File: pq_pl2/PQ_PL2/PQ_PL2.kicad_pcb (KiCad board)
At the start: 4 copper layers, 40 x 40 mm, 79 parts, among them J1 BBL-110-Y-X, J2 BBL-110-Y-X, J3 BBL-110-Y-X, J4 BBL-110-Y-X, J5 U.FL-R-SMT, J6 MS-156C3, J7 MS-156C3, J8 U.FL-R-SMT, U1 LEE2-6+, U2 MAX2121, U4 LT3048, U5 LT071DBV, Y1 ECS-TXO-2016MV

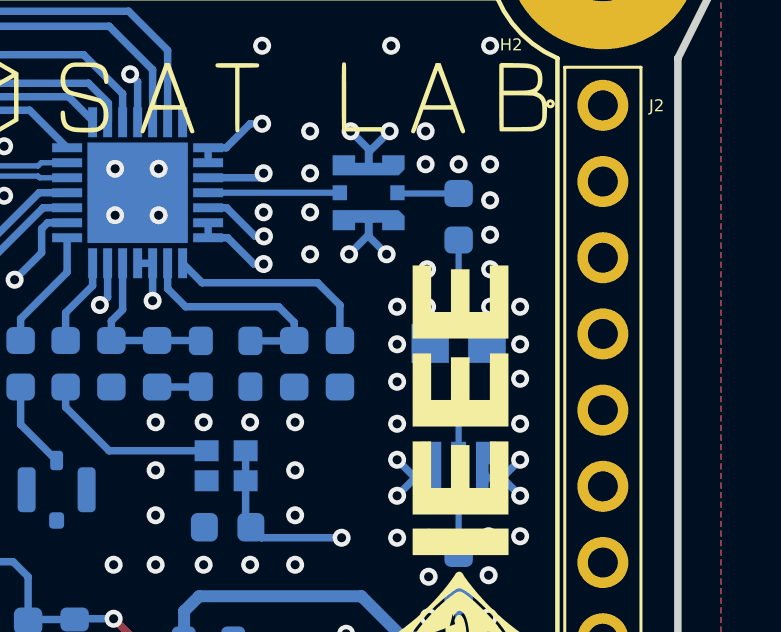
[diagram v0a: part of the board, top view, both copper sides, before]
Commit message: Payload 2 V3.2 - Rounded the RF 90 degree turn between the C3 and J8 probe connector
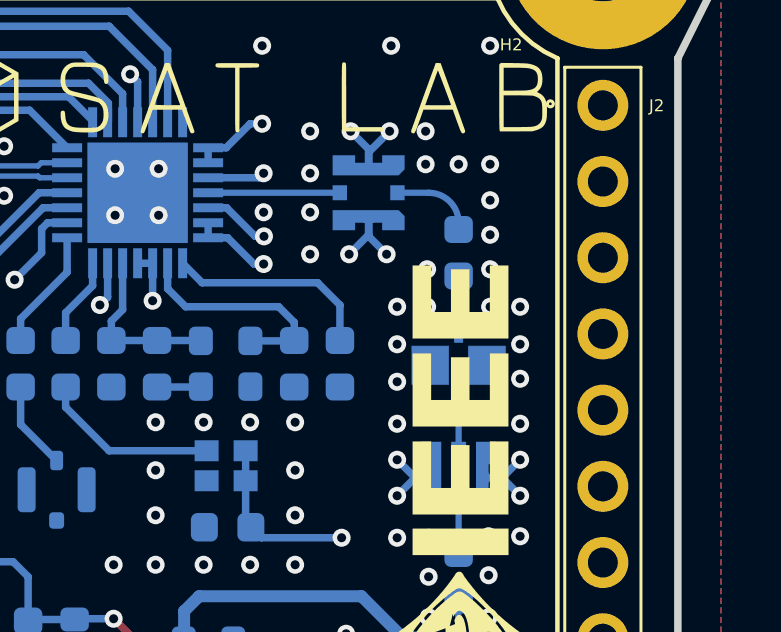
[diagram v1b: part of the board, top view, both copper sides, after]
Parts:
- moved C3 1.20 mm to (114.8, 52.6)
- moved FL1 0.73 mm to (114.8, 56.4)
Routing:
- net RF: track 2.05 -> 2.80 mm
- net Net-(FL1-IN): track 2.11 -> 1.41 mm
- net Net-(FL1-Out): track 2.11 -> 1.60 mm
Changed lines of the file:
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@@
   )
   (footprint "-nsl_rf:GE0805C-3" (layer "B.Cu")
-    (at 114.75 55.625 90)
+    (at 114.75 56.35 90)
     (property "Sheetfile" "PQ_PL2.kicad_sch")
     (property "Sheetname" "")
@@
   )
   (footprint "Capacitor_SMD:C_0603_1608Metric" (layer "B.Cu")
-    (at 114.75 51.4 90)
+    (at 114.75 52.6 90)
     (descr "Capacitor SMD 0603 (1608 Metric), square (rectangular) end terminal, IPC_7351 nominal, (Body size source: IPC-SM-782 page 76, https://www.pcb-3d.com/wordpress/wp-content/uploads/ipc-sm-782a_amendment_1_and_2.pdf), generated with kicad-footprint-generator")
     (tags "capacitor")
@@
   (gr_line locked (start 88.043 46.1172) (end 88.043 72.1172)
     (stroke (width 0.15) (type solid)) (layer "F.SilkS"))
+  (gr_line (start 112.7625 50.6) (end 113.7375 50.6)
+    (stroke (width 0.61) (type default)) (layer "B.Mask"))
   (gr_line (start 114.75 65.6) (end 114.75 66.7)
     (stroke (width 0.64) (type default)) (layer "B.Mask"))
-  (gr_line (start 112.8 50.6) (end 114.875 50.6)
-    (stroke (width 0.64) (type default)) (layer "B.Mask"))
+  (gr_arc (start 113.5 50.565167) (mid 114.462448 50.906475) (end 114.852851 51.850076)
+    (stroke (width 0.6) (type default)) (layer "B.Mask"))
   (gr_line (start 114.75 69.25) (end 114.75 70.35)
     (stroke (width 0.64) (type default)) (layer "B.Mask"))
@@
   (gr_line (start 114.75 61.15) (end 114.75 62.75)
     (stroke (width 0.64) (type default)) (layer "B.Mask"))
-  (gr_line (start 114.75 52.05) (end 114.75 54.55)
+  (gr_line (start 114.75 53.25) (end 114.75 55.3)
     (stroke (width 0.61) (type default)) (layer "B.Mask"))
-  (gr_line (start 114.75 56.7) (end 114.75 59.05)
+  (gr_line (start 114.75 57.4) (end 114.75 59.05)
     (stroke (width 0.64) (type default)) (layer "B.Mask"))
   (gr_line (start 114.75 71.9) (end 114.75 73.05)
@@
   (segment (start 114.7375 65.7) (end 114.7375 64.1875) (width 0.21) (layer "B.Cu") (net 3))
   (segment (start 114.75 61.06) (end 114.75 62.625) (width 0.21) (layer "B.Cu") (net 4))
-  (segment (start 114.75 52.175) (end 114.75 54.28) (width 0.21) (layer "B.Cu") (net 5))
-  (segment (start 114.75 50.625) (end 112.735 50.625) (width 0.21) (layer "B.Cu") (net 6))
-  (segment (start 112.735 50.625) (end 112.71 50.6) (width 0.21) (layer "B.Cu") (net 6))
+  (segment (start 114.75 53.375) (end 114.75 54.975) (width 0.21) (layer "B.Cu") (net 5))
+  (segment (start 113.75 50.6) (end 112.71 50.6) (width 0.21) (layer "B.Cu") (net 6))
+  (segment (start 114.75 51.6) (end 114.75 51.825) (width 0.21) (layer "B.Cu") (net 6))
+  (arc (start 114.75 51.6) (mid 114.457106 50.892893) (end 113.75 50.6) (width 0.21) (layer "B.Cu") (net 6))
   (via (at 103.8 46.65) (size 0.6) (drill 0.3) (layers "F.Cu" "B.Cu") (net 7))
   (via (at 99.95 53.5) (size 0.6) (drill 0.3) (layers "F.Cu" "B.Cu") (net 7))
@@
   (segment (start 107.187 68.59) (end 107.187 67.066) (width 0.4) (layer "B.Cu") (net 31))
   (segment (start 107.187 67.066) (end 107.187 65.581) (width 0.4) (layer "B.Cu") (net 31))
-  (segment (start 114.75 59.14) (end 114.75 57.03) (width 0.21) (layer "B.Cu") (net 32))
+  (segment (start 114.75 57.725) (end 114.75 59.14) (width 0.21) (layer "B.Cu") (net 32))
   (segment (start 103.1 45.05) (end 94.0528 45.05) (width 0.25) (layer "B.Cu") (net 33))
   (segment (start 104.55 48.25) (end 104.55 46.5) (width 0.25) (layer "B.Cu") (net 33))

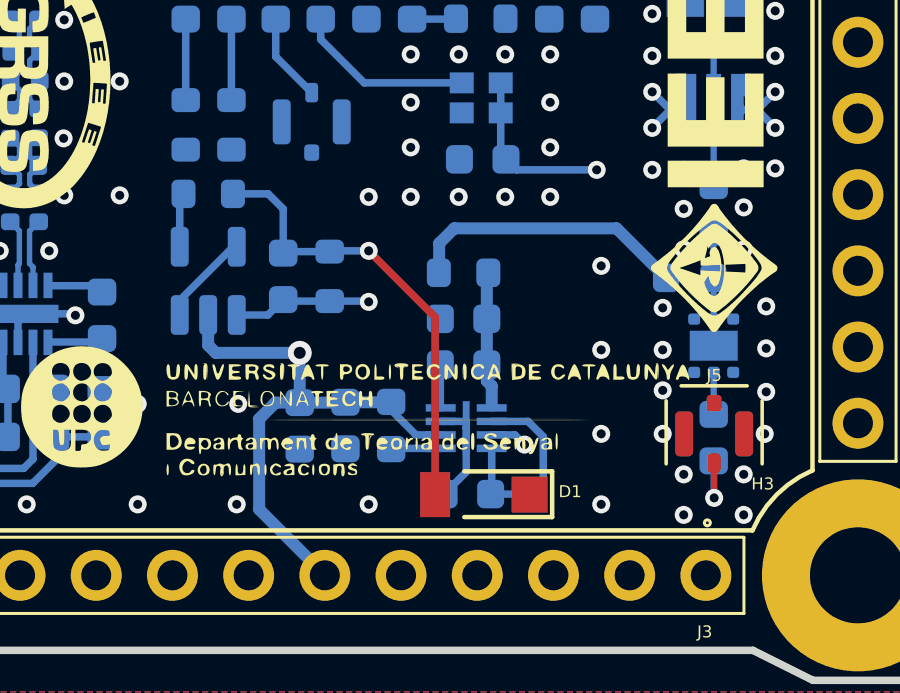
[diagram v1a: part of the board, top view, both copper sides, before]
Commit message: Corrected the PL2 5V booster issue (changed the pins of the LT3048-5 to LT3048 & added resistive divider for 5V output)
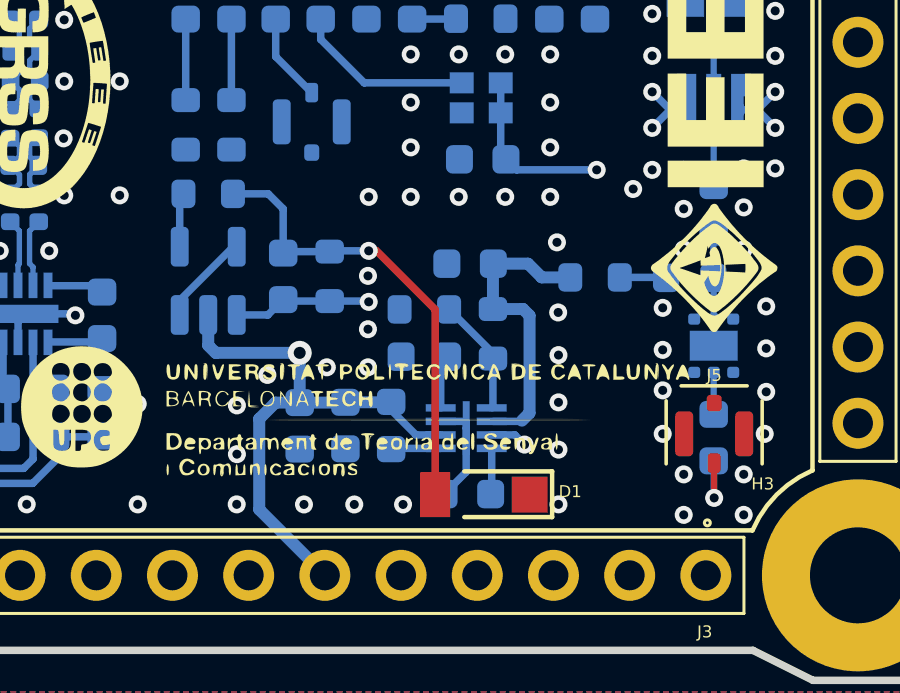
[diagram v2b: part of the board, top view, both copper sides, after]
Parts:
- added R10: 360k, Resistor_SMD:R_0603_1608Metric, B.Cu at (107.4, 67.6)
- added R11: 120k, Resistor_SMD:R_0603_1608Metric, B.Cu at (105.1, 66.8)
- C17, C23: value 310pF -> 300pF
- U3: value ~ -> LT5537
- U5: value LT071DBV -> TL071
- moved R1 4.39 mm to (110.8, 65.7), turned to 0 degrees
- moved C33 1.85 mm to (106.6, 65.2)
- moved C32 1.33 mm to (105.1, 68.3)
- turned C31 to 0 degrees
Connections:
- C31 pad 1: Net-(U4-BSOUT) -> GND
- C31 pad 2: GND -> Net-(U4-BSTOUT)
- C32 pad 1: Net-(U4-BYP) -> GND
- C32 pad 2: 5V -> Net-(U4-BYP)
- U4 pad 5: 5V -> Net-(U4-FB)
- U4 pad 6: Net-(U4-BSOUT) -> 5V
- U4 pad 8: Net-(U4-BSOUT) -> Net-(U4-BSTOUT)
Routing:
- net Net-(L1-Pad1): track 9.44 -> 1.55 mm
- net Net-(U4-BSOUT): track 6.85 -> 0.00 mm
- net 5V: track 4.52 -> 10.1 mm
- net Net-(U4-FB): track 0.00 -> 3.91 mm
- net Net-(U4-BSTOUT): track 0.00 -> 1.54 mm
- net GND: vias 112 -> 123
